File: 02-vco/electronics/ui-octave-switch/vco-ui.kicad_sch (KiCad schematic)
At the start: 32 parts, among them J1 Conn_01x04, J2 Conn_02x05_Odd_Even, J3 Conn_02x03_Odd_Even, J4 Conn_01x02, J5 Conn_02x02_Counter_Clockwise, J6 Conn_01x06, U1 0203

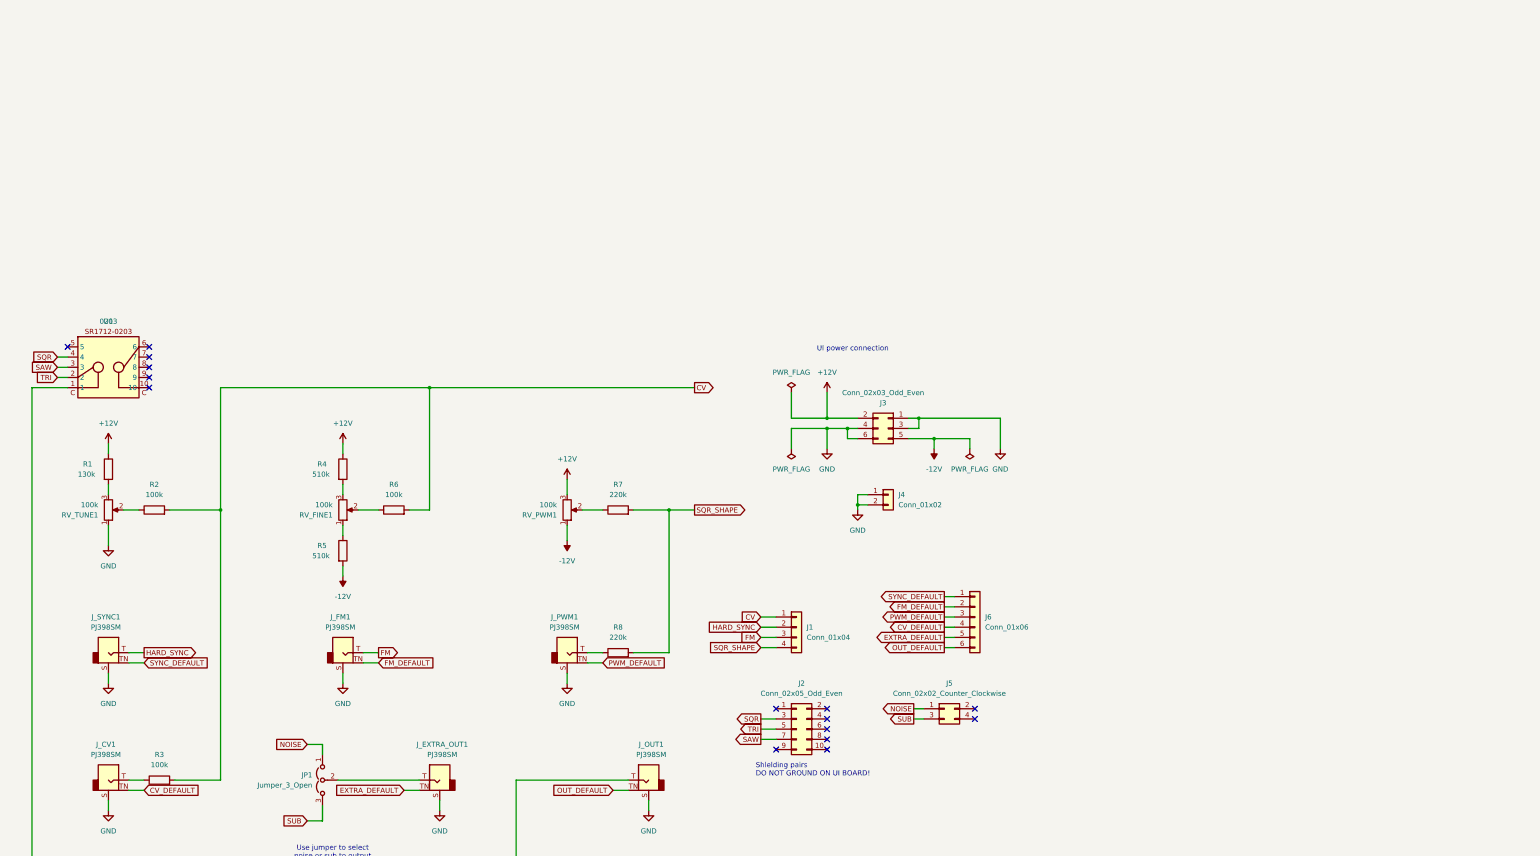
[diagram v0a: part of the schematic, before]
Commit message: WIP of VCO octave switch UI
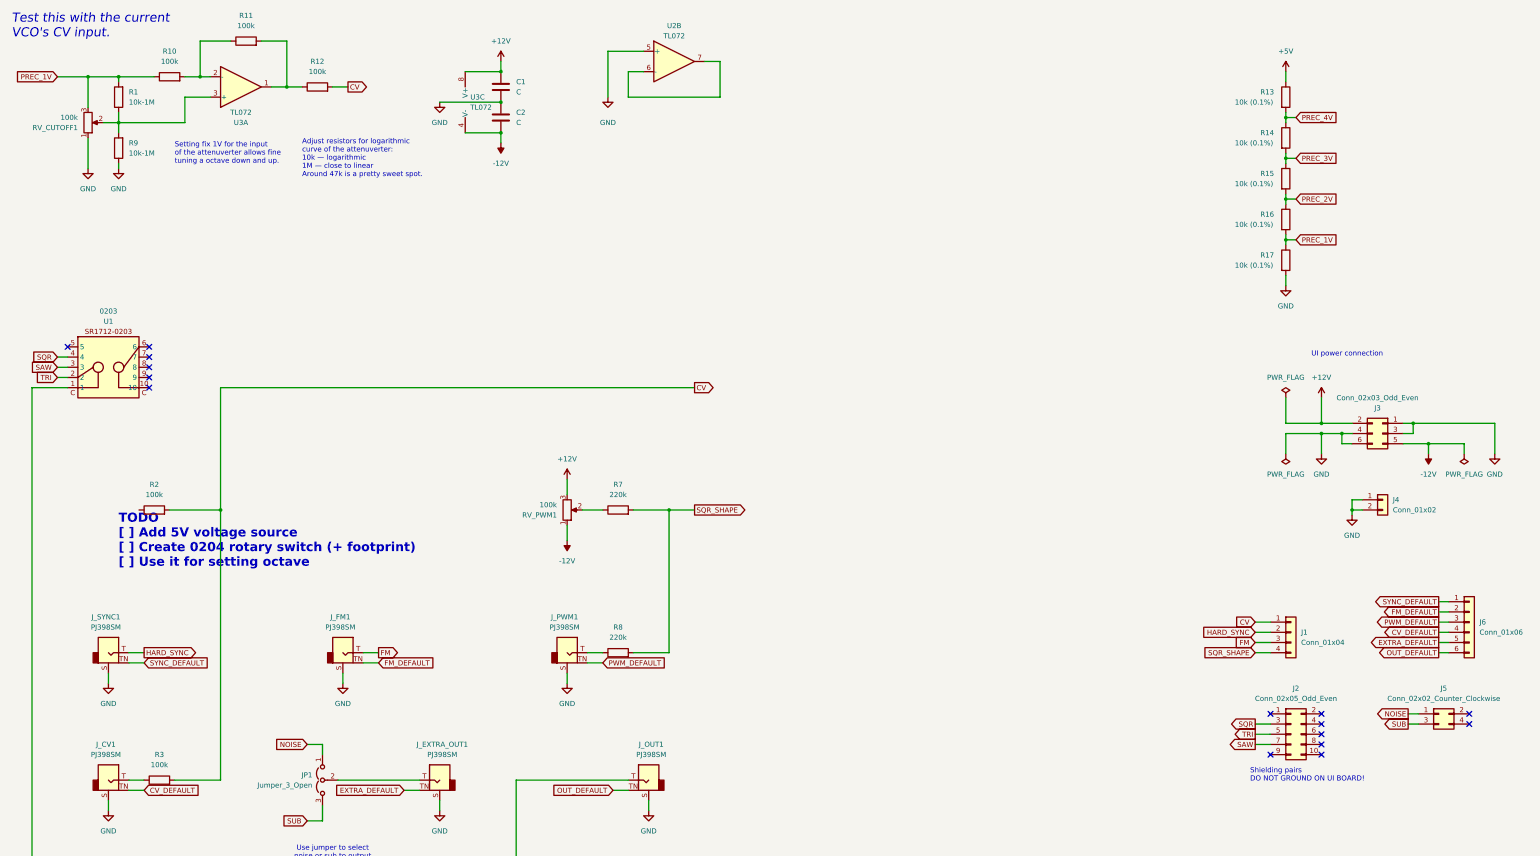
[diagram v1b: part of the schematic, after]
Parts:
- removed R4, R5: 510k, Shmoergh_Custom_Footprints:R_Axial_DIN0207_L6.3mm_D2.5mm_P7.62mm_Horizontal, symbol Device:R
- removed R6: 100k, Shmoergh_Custom_Footprints:R_Axial_DIN0207_L6.3mm_D2.5mm_P7.62mm_Horizontal, symbol Device:R
- removed RV_FINE1: 100k, Shmoergh_Custom_Footprints:Potentiometer_Bourns_Single-PTV09A, symbol Device:R_Potentiometer
- added C1, C2: C, Capacitor_THT:C_Disc_D5.0mm_W2.5mm_P2.50mm, symbol Device:C
- added R10, R11, R12: 100k, Shmoergh_Custom_Footprints:R_Axial_DIN0207_L6.3mm_D2.5mm_P7.62mm_Horizontal, symbol Device:R
- added R13, R14, R15, R16, R17: 10k (0.1%), Shmoergh_Custom_Footprints:R_Axial_DIN0207_L6.3mm_D2.5mm_P7.62mm_Horizontal, symbol Device:R
- added R9: 10k-1M, Shmoergh_Custom_Footprints:R_Axial_DIN0207_L6.3mm_D2.5mm_P7.62mm_Horizontal, symbol Device:R
- added U2, U3: TL072, symbol Amplifier_Operational:TL072
- R1: value 130k -> 10k-1M; Part URL (none) -> https://mou.sr/4hEwI4G; Part no. (none) -> 603-MFR-25FRF52100K
- renumbered RV_TUNE1 to RV_CUTOFF1
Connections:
- net +12V: now also C1.1, U3.8 (V+); no longer R1.1
- net -12V: now also C2.2, U3.4 (V-)
- net CV: now also R12.2
- net GND: now also C1.2, C2.1, R17.2, R9.1, U2.5 (+)
- net PREC_1V: now reaches R1.2, RV_CUTOFF1.3
- net PREC_1V: now also R10.1, R16.2, R17.1
- net at RV_CUTOFF1.2: now also R1.1, R9.2, U3.3 (+); no longer R2.1
- new net: R10.2, R11.1, U3.2 (-)
- new net: R11.2, R12.1, U3.1
- new net: U2.6 (-), U2.7
- new net +5V: R13.1
- new net PREC_2V: R15.2, R16.1
- new net PREC_3V: R14.2, R15.1
- new net PREC_4V: R13.2, R14.1
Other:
- note added: "Adjust resistors for logarithmic curve of the attenuverter: 10k — logarithmic 1M — close to linear Around 47k is a pretty sweet spot."
- note added: "Setting fix 1V for the input of the attenuverter allows fine tuning a octave down and up."
- note added: "TODO [ ] Add 5V voltage source [ ] Create 0204 rotary switch (+ footprint) [ ] Use it for setting octave"
- note added: "Test this with the current VCO's CV input."
- moved on the sheet: J1, J2, J3, J4, J5, J6, RV_CUTOFF1

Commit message: Designed v0.2 VCO UI (with octave switch)
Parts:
- removed JP2, JP3: Jumper_2_Open, Connector_PinHeader_2.54mm:PinHeader_1x02_P2.54mm_Horizontal, symbol Jumper:Jumper_2_Open
- removed R13, R14, R15, R16, R17: 10k (0.1%), Shmoergh_Custom_Footprints:R_Axial_DIN0207_L6.3mm_D2.5mm_P7.62mm_Horizontal, symbol Device:R
- added U1: 0204, Shmoergh_Custom_Footprints:SR1712-0204, symbol Shmoergh-Custom-Components:SR1712_0204
- U2: renamed from U3; footprint (none) -> Package_DIP:DIP-8_W7.62mm_LongPads
- U2: footprint (none) -> Package_DIP:DIP-8_W7.62mm_LongPads
- renumbered R3 to R1, R1 to R2, R9 to R3, R2 to R4, R10 to R5, R11 to R6, R12 to R7, R7 to R8, R8 to R9, RV_CUTOFF1 to RV_FINE_TUNE1, U1 to U3
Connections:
- net CV: now also R4.1; no longer R4.2
- net GND: now also U1.2
- net NOISE: now also JP1.3 (B); no longer JP1.1 (A)
- net PREC_1V: now also U1.3
- net PREC_2V: now also U1.4
- net PREC_3V: now also U1.5
- net SUB: now also JP1.1 (A); no longer JP1.3 (B)
- new net: R4.2, U1.1
- no-connect marks 15 -> 20
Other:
- added sheet 5V Source (sheets/5v-source.kicad_sch)
- note removed: "TODO [ ] Add 5V voltage source [ ] Create 0204 rotary switch (+ footprint) [ ] Use it for setting octave"
- note removed: "Use these jumpers to ground critical default inputs to ground if needed."
- moved on the sheet: C1, C2, J1, J2, J3, J4, J5, J6, JP1, J_CV1, J_EXTRA_OUT1, J_FM1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

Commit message: Added VCO output to default connector
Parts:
- J6: value Conn_01x06 -> Conn_01x07; footprint Connector_PinSocket_2.54mm:PinSocket_1x06_P2.54mm_Vertical -> Connector_PinSocket_2.54mm:PinSocket_1x07_P2.54mm_Vertical; symbol Connector_Generic:Conn_01x06 -> Connector_Generic:Conn_01x07
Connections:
- net OUT_DEFAULT: now also J6.7 (Pin_7); no longer J6.6 (Pin_6)
- net OUT_OUT: now reaches J_OUT1.T, U3.1
- net OUT_OUT: now also J6.6 (Pin_6)
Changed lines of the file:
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@@
 	)
 	(junction
+		(at 133.35 109.22)
+		(diameter 0)
+		(color 0 0 0 0)
+	)
+	(junction
 		(at 143.51 49.53)
 		(diameter 0)
@@
 	(wire
 		(pts
+			(xy 133.35 106.68) (xy 133.35 109.22)
+		)
+		(stroke
+			(width 0)
+			(type default)
+		)
+	)
+	(wire
+		(pts
 			(xy 87.63 175.26) (xy 91.44 175.26)
 		)
@@
 	(wire
 		(pts
-			(xy 107.95 109.22) (xy 134.62 109.22)
+			(xy 107.95 109.22) (xy 133.35 109.22)
+		)
+		(stroke
+			(width 0)
+			(type default)
+		)
+	)
+	(wire
+		(pts
+			(xy 130.81 106.68) (xy 133.35 106.68)
 		)
 		(stroke
@@
 	(wire
 		(pts
+			(xy 133.35 109.22) (xy 134.62 109.22)
+		)
+		(stroke
+			(width 0)
+			(type default)
+		)
+	)
+	(wire
+		(pts
 			(xy 229.87 138.43) (xy 234.95 138.43)
 		)
@@
 	(wire
 		(pts
+			(xy 245.11 41.91) (xy 247.65 41.91)
+		)
+		(stroke
+			(width 0)
+			(type default)
+		)
+	)
+	(wire
+		(pts
 			(xy 179.07 139.7) (xy 179.07 142.24)
 		)
@@
 		)
 	)
+	(global_label "OUT_OUT"
+		(shape input)
+		(at 130.81 106.68 180)
+		(fields_autoplaced yes)
+		(effects
+			(font
+				(size 1.27 1.27)
+			)
+			(justify right)
+		)
+		(property "Intersheetrefs" "${INTERSHEET_REFS}"
+			(at 119.6 106.68 0)
+			(effects
+				(font
+					(size 1.27 1.27)
+				)
+				(justify right)
+				(hide yes)
+			)
+		)
+	)
 	(global_label "CV"
 		(shape input)
@@
 	(global_label "OUT_DEFAULT"
 		(shape output)
-		(at 245.11 39.37 180)
+		(at 245.11 41.91 180)
 		(fields_autoplaced yes)
 		(effects
@@
 		)
 		(property "Intersheetrefs" "${INTERSHEET_REFS}"
-			(at 229.6062 39.37 0)
+			(at 229.6062 41.91 0)
 			(effects
 				(font
@@
 		)
 	)
+	(global_label "OUT_OUT"
+		(shape output)
+		(at 245.11 39.37 180)
+		(fields_autoplaced yes)
+		(effects
+			(font
+				(size 1.27 1.27)
+			)
+			(justify right)
+		)
+		(property "Intersheetrefs" "${INTERSHEET_REFS}"
+			(at 233.9 39.37 0)
+			(effects
+				(font
+					(size 1.27 1.27)
+				)
+				(justify right)
+				(hide yes)
+			)
+		)
+	)
 	(symbol
 		(lib_id "power:GND")
@@
 	)
 	(symbol
-		(lib_id "Connector_Generic:Conn_01x06")
-		(at 252.73 31.75 0)
+		(lib_id "Connector_Generic:Conn_01x07")
+		(at 252.73 34.29 0)
 		(unit 1)
 		(exclude_from_sim no)
@@
 		(fields_autoplaced yes)
 		(property "Reference" "J6"
-			(at 255.27 31.7499 0)
+			(at 255.27 33.0199 0)
 			(effects
 				(font
@@
 			)
 		)
-		(property "Value" "Conn_01x06"
-			(at 255.27 34.2899 0)
+		(property "Value" "Conn_01x07"
+			(at 255.27 35.5599 0)
 			(effects
 				(font
@@
 			)
 		)
-		(property "Footprint" "Connector_PinSocket_2.54mm:PinSocket_1x06_P2.54mm_Vertical"
-			(at 252.73 31.75 0)
+		(property "Footprint" "Connector_PinSocket_2.54mm:PinSocket_1x07_P2.54mm_Vertical"
+			(at 252.73 34.29 0)
 			(effects
 				(font
@@
 		)
 		(property "Datasheet" "~"
-			(at 252.73 31.75 0)
+			(at 252.73 34.29 0)
 			(effects
 				(font
@@
 			)
 		)
-		(property "Description" "Generic connector, single row, 01x06, script generated (kicad-library-utils/schlib/autogen/connector/)"
-			(at 252.73 31.75 0)
+		(property "Description" "Generic connector, single row, 01x07, script generated (kicad-library-utils/schlib/autogen/connector/)"
+			(at 252.73 34.29 0)
 			(effects
 				(font
@@
 		)
 		(property "Part URL" "https://mou.sr/4lnf48h"
-			(at 252.73 31.75 0)
+			(at 252.73 34.29 0)
 			(effects
 				(font
@@
 		)
 		(property "Vendor" "Mouser"
-			(at 252.73 31.75 0)
+			(at 252.73 34.29 0)
 			(effects
 				(font
@@
 		)
 		(property "LCSC" ""
-			(at 252.73 31.75 0)
+			(at 252.73 34.29 0)
 			(effects
 				(font
@@
 		)
 		(property "Part no." "200-SSW10601TS"
-			(at 252.73 31.75 0)
+			(at 252.73 34.29 0)
+			(effects
+				(font
+					(size 1.27 1.27)
+				)
+				(hide yes)
+			)
+		)
+		(property "Part No." ""
+			(at 252.73 34.29 0)
 			(effects
 				(font
@@
 		(pin "5"
 		)
+		(pin "7"
+		)
 		(instances

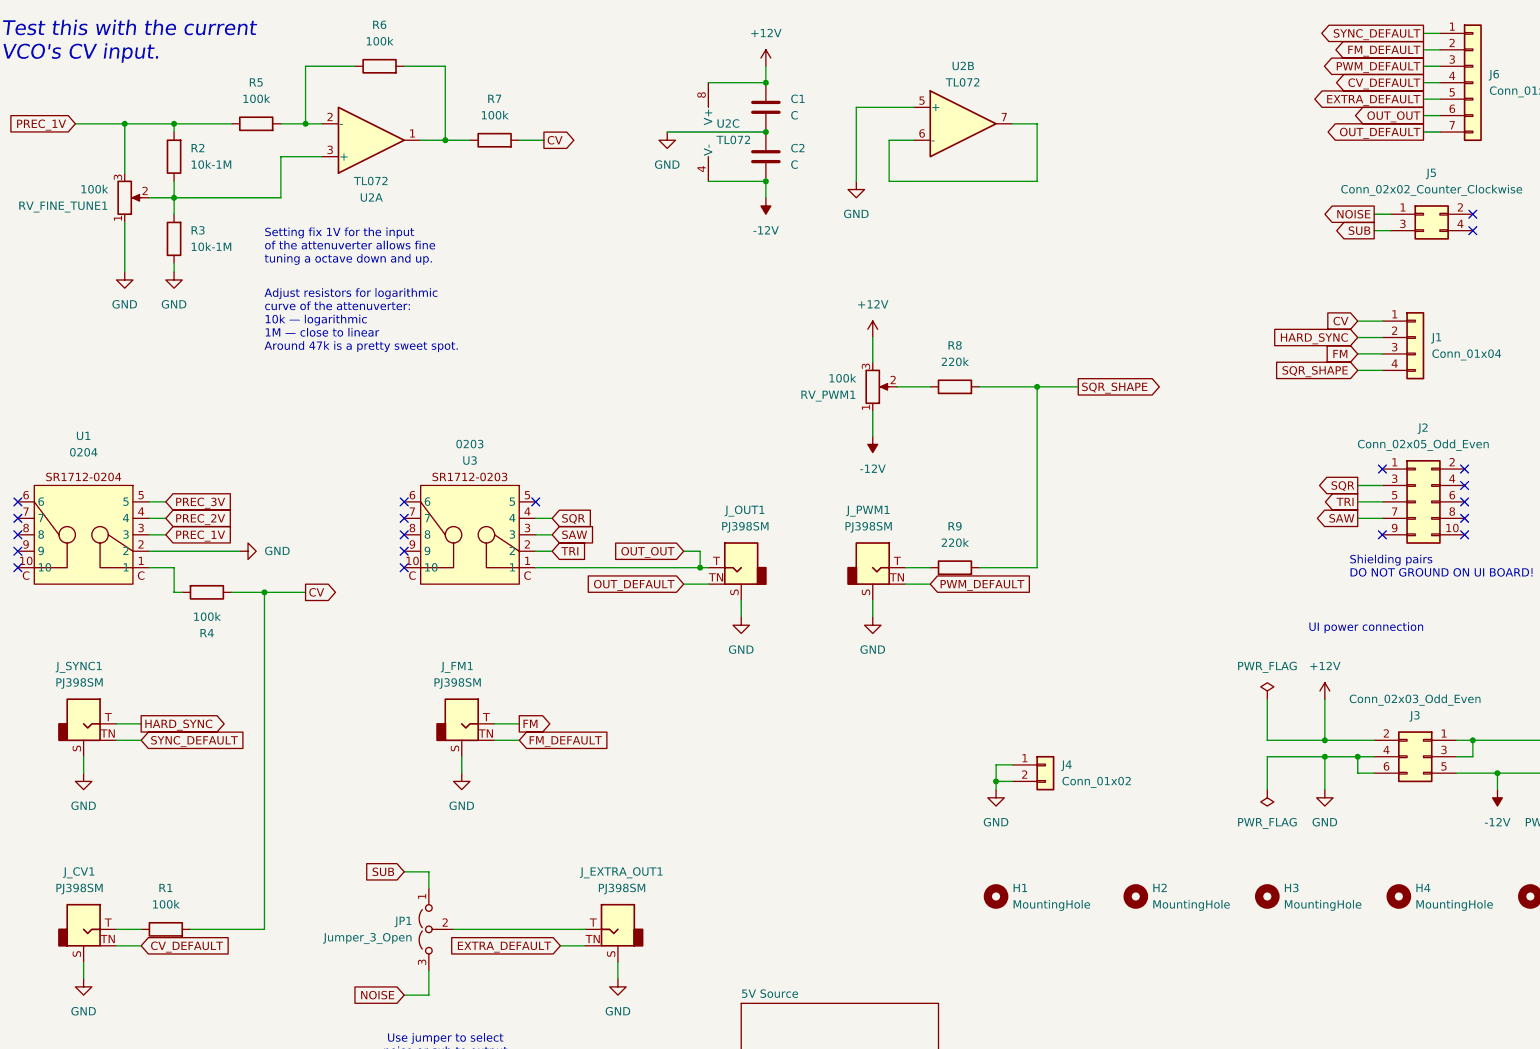
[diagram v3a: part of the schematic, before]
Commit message: Added CV output to VCO default patch
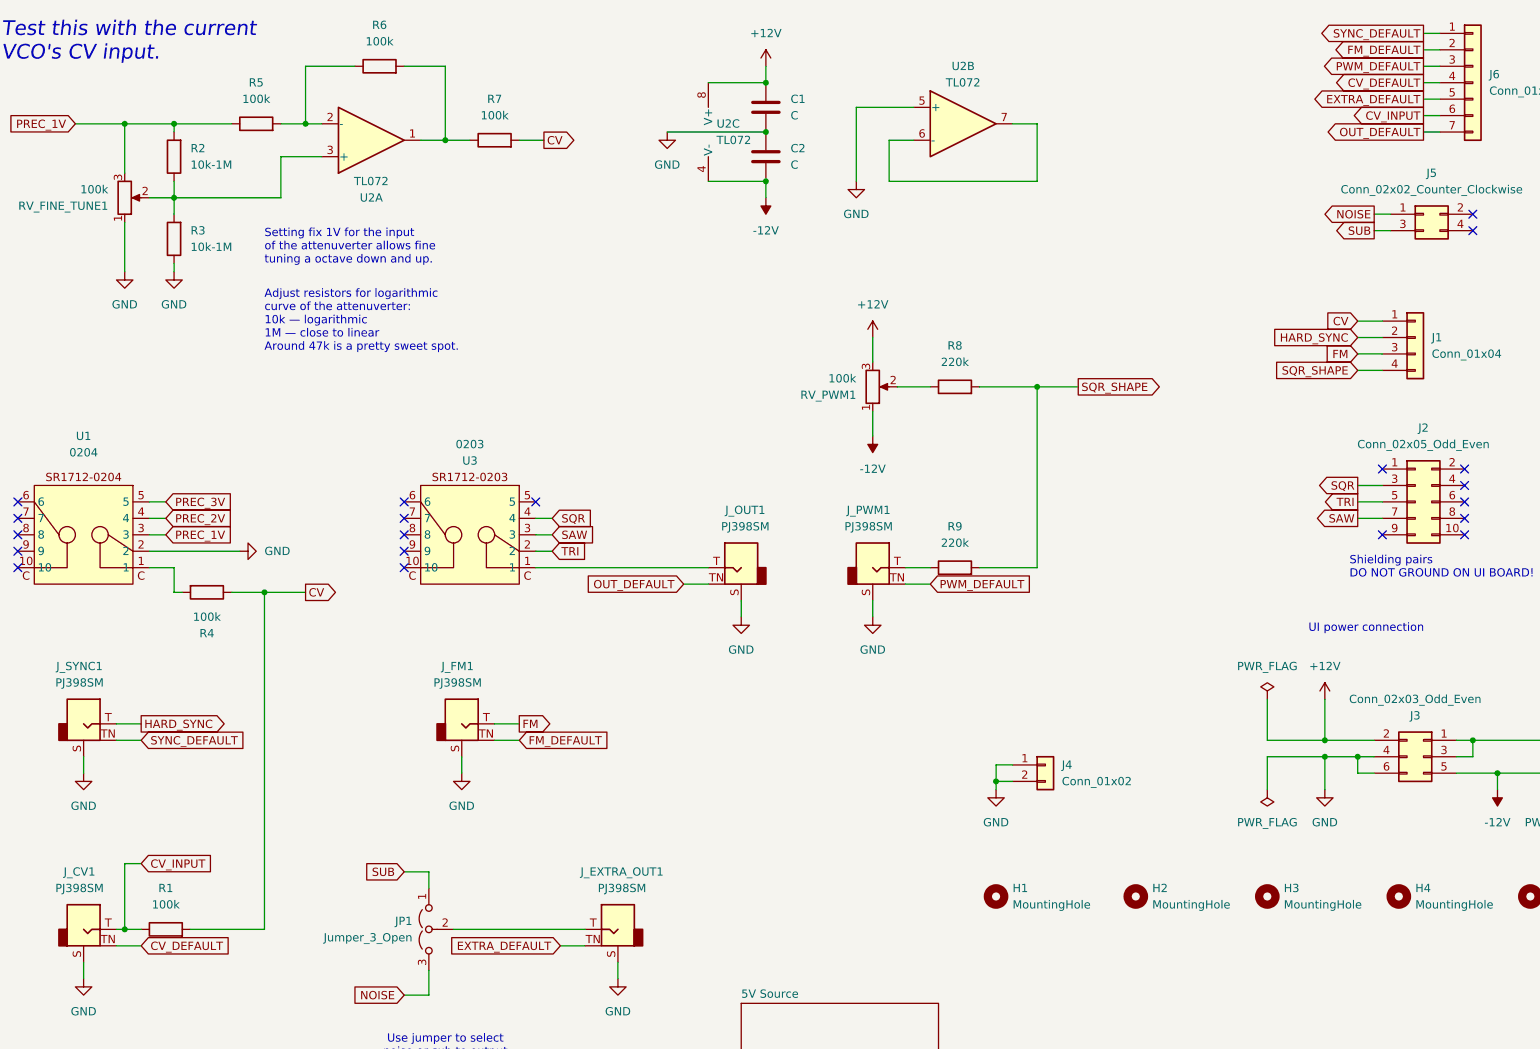
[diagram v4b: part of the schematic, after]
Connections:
- net CV_INPUT: now reaches J_CV1.T, R1.1
- net CV_INPUT: now also J6.6 (Pin_6)
- net OUT_OUT: no longer names the net of J_OUT1.T, U3.1
- net OUT_OUT: no longer J6.6 (Pin_6)
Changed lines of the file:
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@@
-	)
-	(junction
-		(at 133.35 109.22)
-		(diameter 0)
-		(color 0 0 0 0)
 	)
 	(junction
@@
 		(color 0 0 0 0)
 	)
+	(junction
+		(at 44.45 165.1)
+		(diameter 0)
+		(color 0 0 0 0)
+	)
 	(no_connect
 		(at 251.46 104.14)
@@
 	(wire
 		(pts
-			(xy 133.35 106.68) (xy 133.35 109.22)
-		)
-		(stroke
-			(width 0)
-			(type default)
-		)
-	)
-	(wire
-		(pts
 			(xy 87.63 175.26) (xy 91.44 175.26)
 		)
@@
 	(wire
 		(pts
-			(xy 107.95 109.22) (xy 133.35 109.22)
-		)
-		(stroke
-			(width 0)
-			(type default)
-		)
-	)
-	(wire
-		(pts
-			(xy 130.81 106.68) (xy 133.35 106.68)
+			(xy 107.95 109.22) (xy 134.62 109.22)
 		)
 		(stroke
@@
 	(wire
 		(pts
+			(xy 44.45 154.94) (xy 44.45 165.1)
+		)
+		(stroke
+			(width 0)
+			(type default)
+		)
+	)
+	(wire
+		(pts
 			(xy 87.63 156.21) (xy 91.44 156.21)
 		)
@@
 	(wire
 		(pts
+			(xy 44.45 165.1) (xy 43.18 165.1)
+		)
+		(stroke
+			(width 0)
+			(type default)
+		)
+	)
+	(wire
+		(pts
 			(xy 157.48 38.1) (xy 157.48 49.53)
 		)
@@
 	(wire
 		(pts
-			(xy 133.35 109.22) (xy 134.62 109.22)
-		)
-		(stroke
-			(width 0)
-			(type default)
-		)
-	)
-	(wire
-		(pts
 			(xy 229.87 138.43) (xy 234.95 138.43)
 		)
@@
 	(wire
 		(pts
+			(xy 46.99 154.94) (xy 44.45 154.94)
+		)
+		(stroke
+			(width 0)
+			(type default)
+		)
+	)
+	(wire
+		(pts
 			(xy 229.87 129.54) (xy 229.87 135.89)
 		)
@@
 	(wire
 		(pts
-			(xy 46.99 165.1) (xy 43.18 165.1)
+			(xy 46.99 165.1) (xy 44.45 165.1)
 		)
 		(stroke
@@
 		)
 	)
-	(global_label "OUT_OUT"
+	(global_label "CV_INPUT"
 		(shape input)
-		(at 130.81 106.68 180)
-		(fields_autoplaced yes)
-		(effects
-			(font
-				(size 1.27 1.27)
-			)
-			(justify right)
-		)
-		(property "Intersheetrefs" "${INTERSHEET_REFS}"
-			(at 119.6 106.68 0)
-			(effects
-				(font
-					(size 1.27 1.27)
-				)
-				(justify right)
+		(at 46.99 154.94 0)
+		(fields_autoplaced yes)
+		(effects
+			(font
+				(size 1.27 1.27)
+			)
+			(justify left)
+		)
+		(property "Intersheetrefs" "${INTERSHEET_REFS}"
+			(at 58.8048 154.94 0)
+			(effects
+				(font
+					(size 1.27 1.27)
+				)
+				(justify left)
 				(hide yes)
 			)
@@
 		)
 	)
-	(global_label "OUT_OUT"
+	(global_label "CV_INPUT"
 		(shape output)
 		(at 245.11 39.37 180)
@@
 		)
 		(property "Intersheetrefs" "${INTERSHEET_REFS}"
-			(at 233.9 39.37 0)
-			(effects
-				(font
+			(at 233.2952 39.37 0)
+			(effects
+				(font
